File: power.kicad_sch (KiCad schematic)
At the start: 60 parts, among them J4 Conn_01x02, J5 Conn_01x02, J6 Conn_01x02, Q29 AO3401, Q30 Q_NPN_BEC, T1 COMMON_MODE_CHOKE, U14 NJM2845DL1-3.3, U19 TPS54428DDA, U2 TPS54202

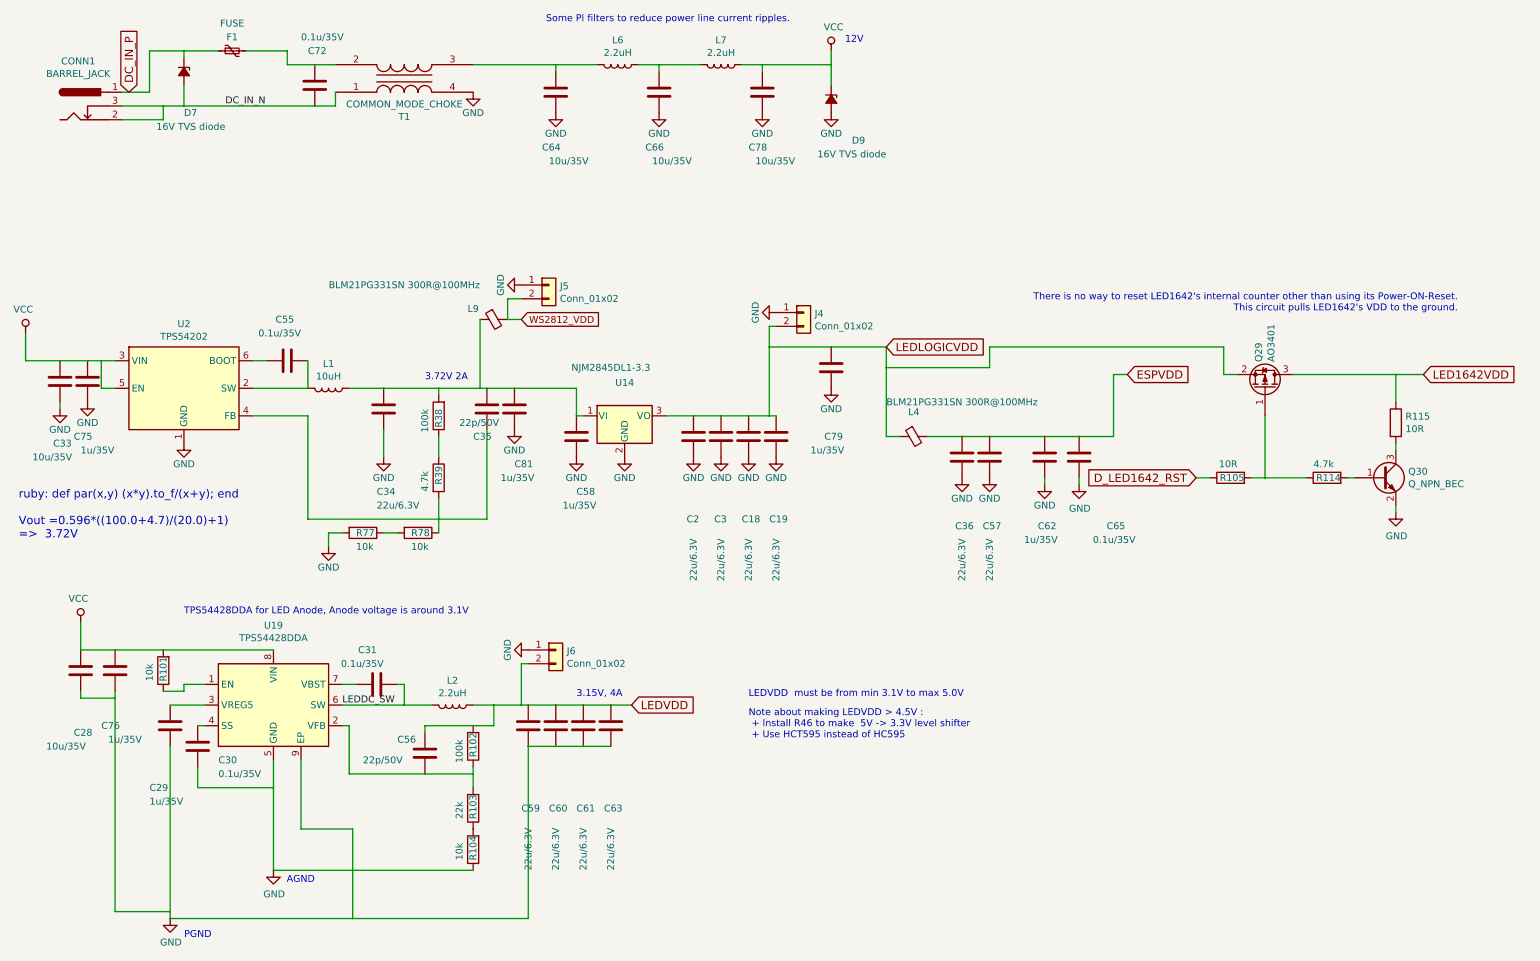
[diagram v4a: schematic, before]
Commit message: Added a schematic comments; I don't know why other files are updated
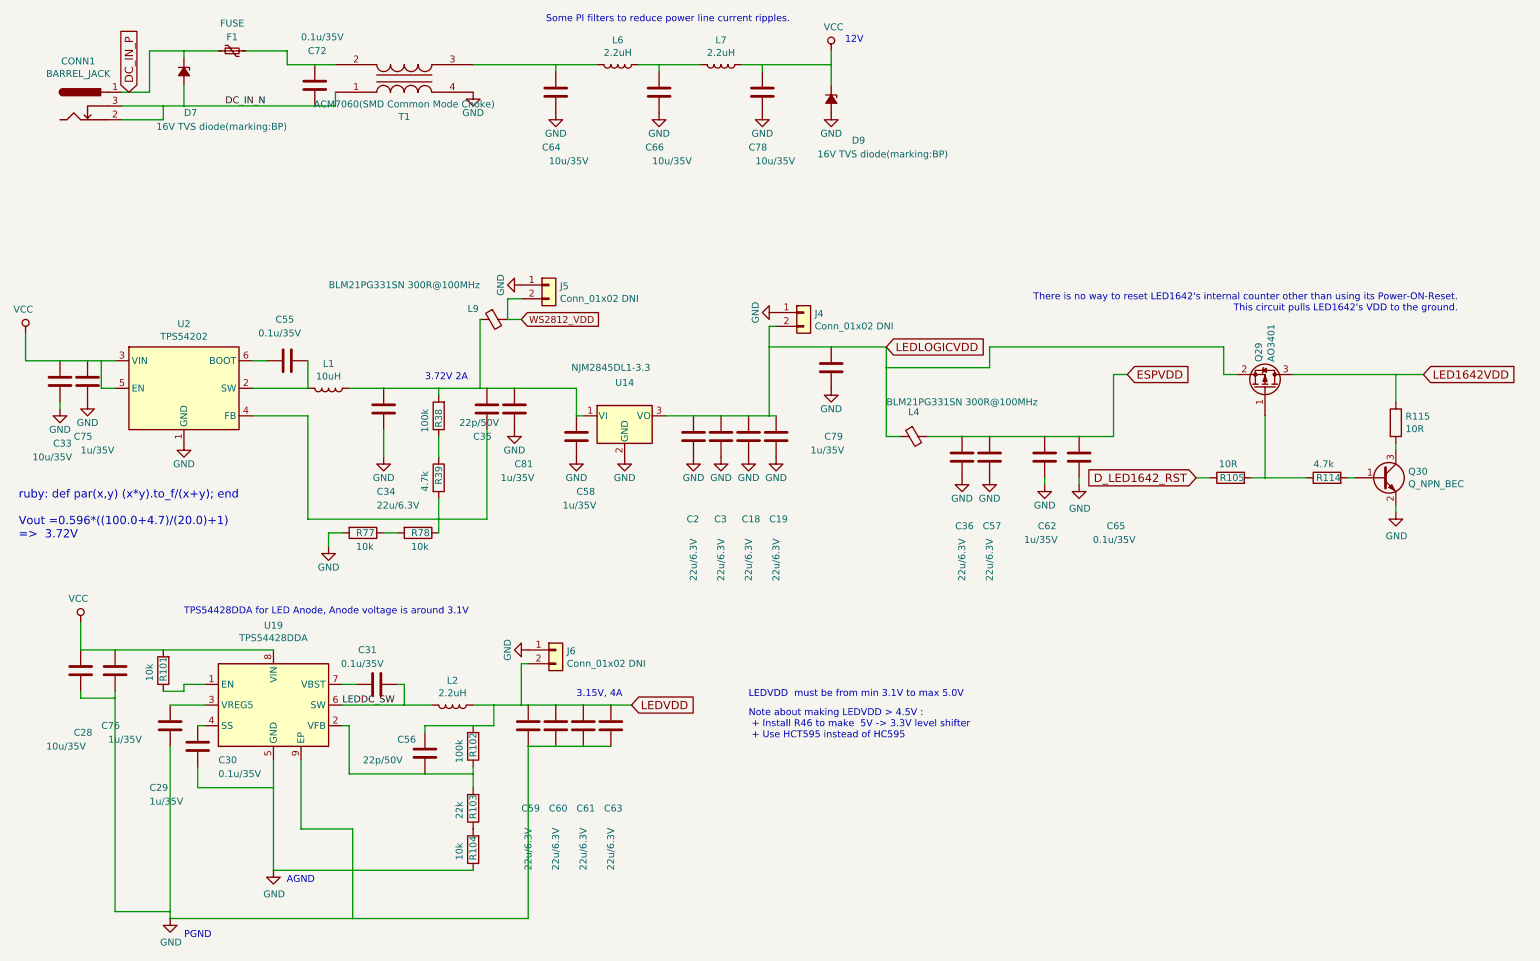
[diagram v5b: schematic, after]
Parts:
- D7, D9: value 16V TVS diode -> 16V TVS diode(marking:BP)
- J4, J5, J6: value Conn_01x02 -> Conn_01x02 DNI
- T1: value COMMON_MODE_CHOKE -> ACM7060(SMD Common Mode Choke)
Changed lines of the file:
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@@
 (kicad_sch (version 20201015) (generator eeschema)
-  (page 1 10)
   (paper "A4")
   (junction (at 21.59 81.28) (diameter 0.3048) (color 0 0 0 0))
@@
     (effects (font (size 1.27 1.27)) (justify left bottom))
   )
-  (global_label "DC_IN_P" (shape input) (at 34.29 31.75 90)
+  (global_label "DC_IN_P" (shape input) (at 34.29 31.75 90)    (property "Intersheet References" "${INTERSHEET_REFS}" (id 0) (at 0 0 0)
+      (effects (font (size 1.27 1.27)) hide)
+    )
     (effects (font (size 1.524 1.524)) (justify left))
   )
-  (global_label "WS2812_VDD" (shape input) (at 106.68 73.66 0)
+  (global_label "WS2812_VDD" (shape input) (at 106.68 73.66 0)    (property "Intersheet References" "${INTERSHEET_REFS}" (id 0) (at 0 0 0)
+      (effects (font (size 1.27 1.27)) hide)
+    )
     (effects (font (size 1.27 1.27)) (justify left))
   )
-  (global_label "LEDVDD" (shape input) (at 127 144.78 0)
+  (global_label "LEDVDD" (shape input) (at 127 144.78 0)    (property "Intersheet References" "${INTERSHEET_REFS}" (id 0) (at 0 0 0)
+      (effects (font (size 1.27 1.27)) hide)
+    )
     (effects (font (size 1.524 1.524)) (justify left))
   )
-  (global_label "LEDLOGICVDD" (shape input) (at 173.99 78.74 0)
+  (global_label "LEDLOGICVDD" (shape input) (at 173.99 78.74 0)    (property "Intersheet References" "${INTERSHEET_REFS}" (id 0) (at 0 0 0)
+      (effects (font (size 1.27 1.27)) hide)
+    )
     (effects (font (size 1.524 1.524)) (justify left))
   )
-  (global_label "ESPVDD" (shape input) (at 218.44 83.82 0)
+  (global_label "ESPVDD" (shape input) (at 218.44 83.82 0)    (property "Intersheet References" "${INTERSHEET_REFS}" (id 0) (at 0 0 0)
+      (effects (font (size 1.27 1.27)) hide)
+    )
     (effects (font (size 1.524 1.524)) (justify left))
   )
-  (global_label "D_LED1642_RST" (shape input) (at 231.14 102.87 180)
+  (global_label "D_LED1642_RST" (shape input) (at 231.14 102.87 180)    (property "Intersheet References" "${INTERSHEET_REFS}" (id 0) (at 0 0 0)
+      (effects (font (size 1.27 1.27)) hide)
+    )
     (effects (font (size 1.524 1.524)) (justify right))
   )
-  (global_label "LED1642VDD" (shape input) (at 273.05 83.82 0)
+  (global_label "LED1642VDD" (shape input) (at 273.05 83.82 0)    (property "Intersheet References" "${INTERSHEET_REFS}" (id 0) (at 0 0 0)
+      (effects (font (size 1.27 1.27)) hide)
+    )
     (effects (font (size 1.524 1.524)) (justify left))
   )
@@
       (effects (font (size 1.27 1.27)) (justify left))
     )
-    (property "Value" "16V TVS diode" (id 1) (at 39.37 38.1 90)
+    (property "Value" "16V TVS diode(marking:BP)" (id 1) (at 39.37 38.1 90)
       (effects (font (size 1.27 1.27)) (justify left))
     )
@@
       (effects (font (size 1.27 1.27)) (justify left))
     )
-    (property "Value" "16V TVS diode" (id 1) (at 161.29 43.18 90)
+    (property "Value" "16V TVS diode(marking:BP)" (id 1) (at 161.29 43.18 90)
       (effects (font (size 1.27 1.27)) (justify left))
     )
@@
       (effects (font (size 1.27 1.27)) (justify left))
     )
-    (property "Value" "Conn_01x02" (id 1) (at 113.792 69.8246 0)
+    (property "Value" "Conn_01x02 DNI" (id 1) (at 113.792 69.825 0)
       (effects (font (size 1.27 1.27)) (justify left))
     )
@@
       (effects (font (size 1.27 1.27)) (justify left))
     )
-    (property "Value" "Conn_01x02" (id 1) (at 115.062 137.1346 0)
+    (property "Value" "Conn_01x02 DNI" (id 1) (at 115.062 137.135 0)
       (effects (font (size 1.27 1.27)) (justify left))
     )
@@
       (effects (font (size 1.27 1.27)) (justify left))
     )
-    (property "Value" "Conn_01x02" (id 1) (at 160.782 74.9046 0)
+    (property "Value" "Conn_01x02 DNI" (id 1) (at 160.782 74.905 0)
       (effects (font (size 1.27 1.27)) (justify left))
     )
@@
     (in_bom yes) (on_board yes)
     (property "Reference" "T1" (id 0) (at 85.09 36.2712 0))
-    (property "Value" "COMMON_MODE_CHOKE" (id 1) (at 85.09 33.9598 0))
+    (property "Value" "ACM7060(SMD Common Mode Choke)" (id 1) (at 85.09 33.9598 0))
     (property "Footprint" "components:Choke_COMMON_SMD_ACM7060" (id 2) (at 85.09 29.21 90)
       (effects (font (size 1.27 1.27)) hide)

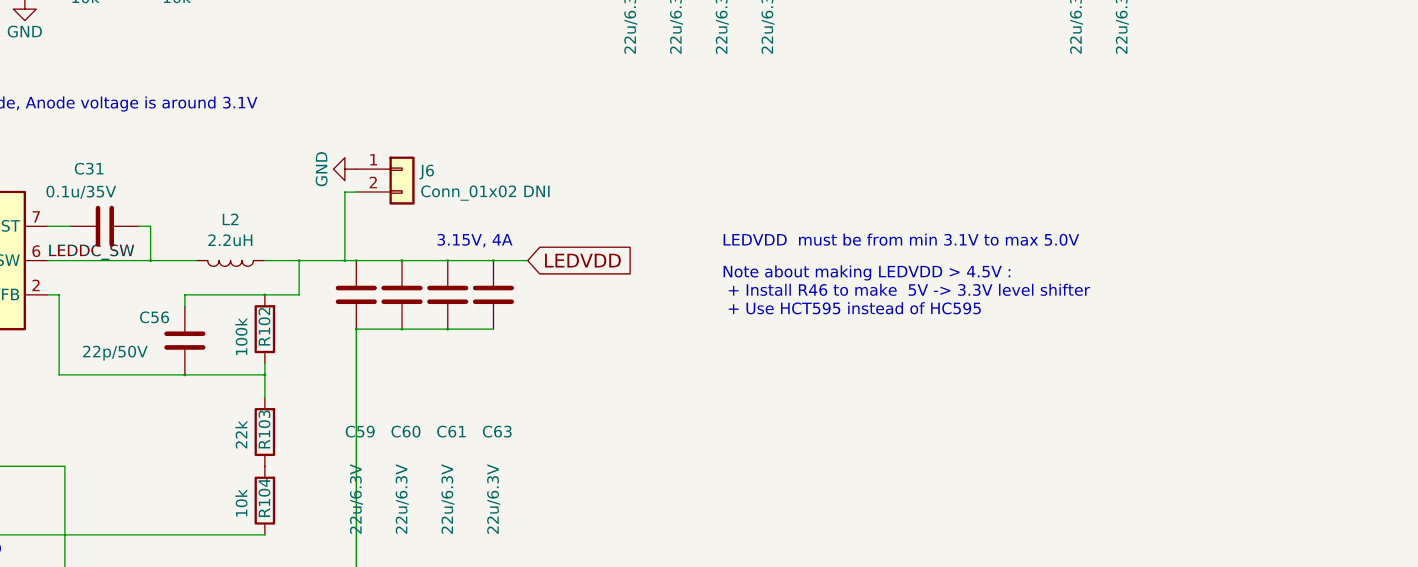
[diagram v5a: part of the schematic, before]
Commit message: Changed L2 value from 2.2uH to '2.2 ~ 6.8uH'
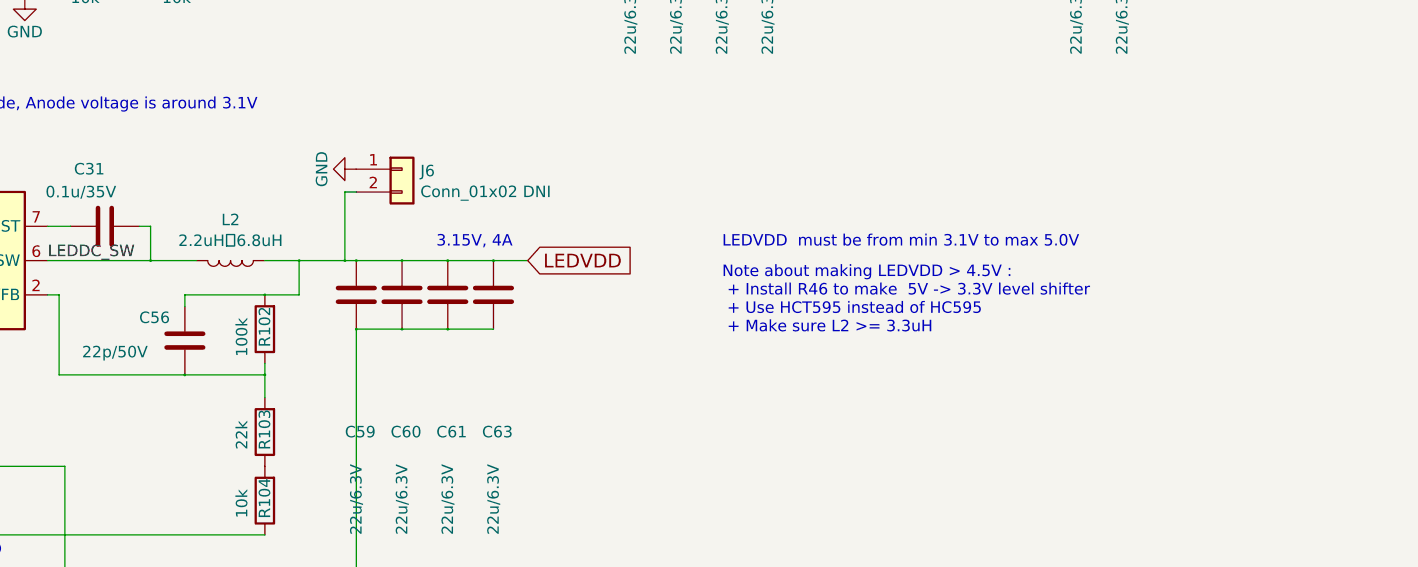
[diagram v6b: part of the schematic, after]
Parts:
- L2: value 2.2uH -> 2.2uH〜6.8uH
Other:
- note added: "Note about making LEDVDD > 4.5V : + Install R46 to make 5V -> 3.3V level shifter + Use HCT595 instead of HC595 + Make sure L2 >= 3.3uH"
- note removed: "Note about making LEDVDD > 4.5V : + Install R46 to make 5V -> 3.3V level shifter + Use HCT595 instead of HC595"

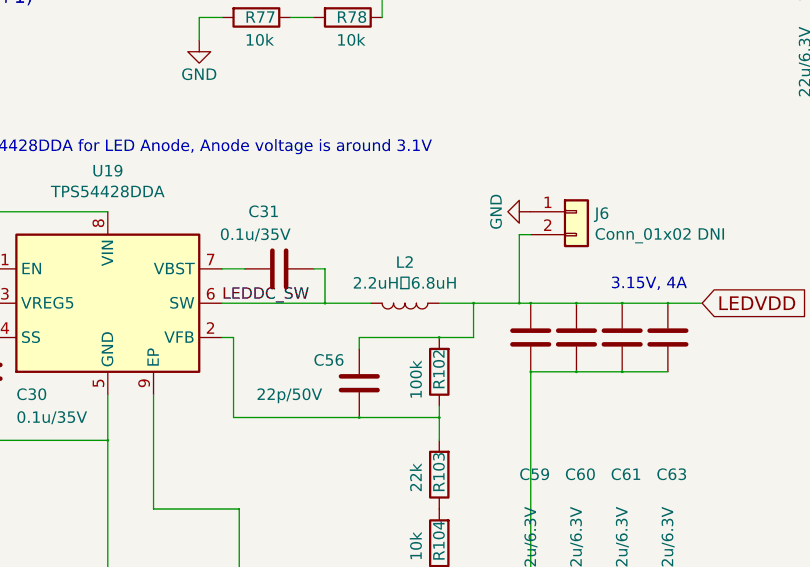
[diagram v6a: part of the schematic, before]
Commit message: Settled L2 value to 6.8uH
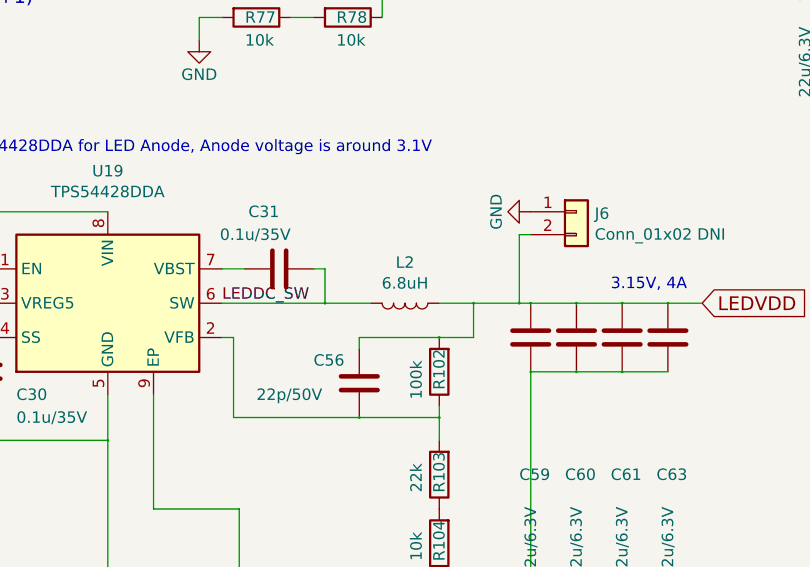
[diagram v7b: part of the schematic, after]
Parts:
- L2: value 2.2uH〜6.8uH -> 6.8uH
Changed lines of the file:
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@@
     (in_bom yes) (on_board yes)
     (property "Reference" "L2" (id 0) (at 93.98 140.2588 90))
-    (property "Value" "2.2uH〜6.8uH" (id 1) (at 93.98 142.57 90))
+    (property "Value" "6.8uH" (id 1) (at 93.98 142.57 90))
     (property "Footprint" "components:Choke_SMD_10.4x10.4_H4.8_HandSoldering" (id 2) (at 93.98 144.78 0)
       (effects (font (size 1.27 1.27)) hide)

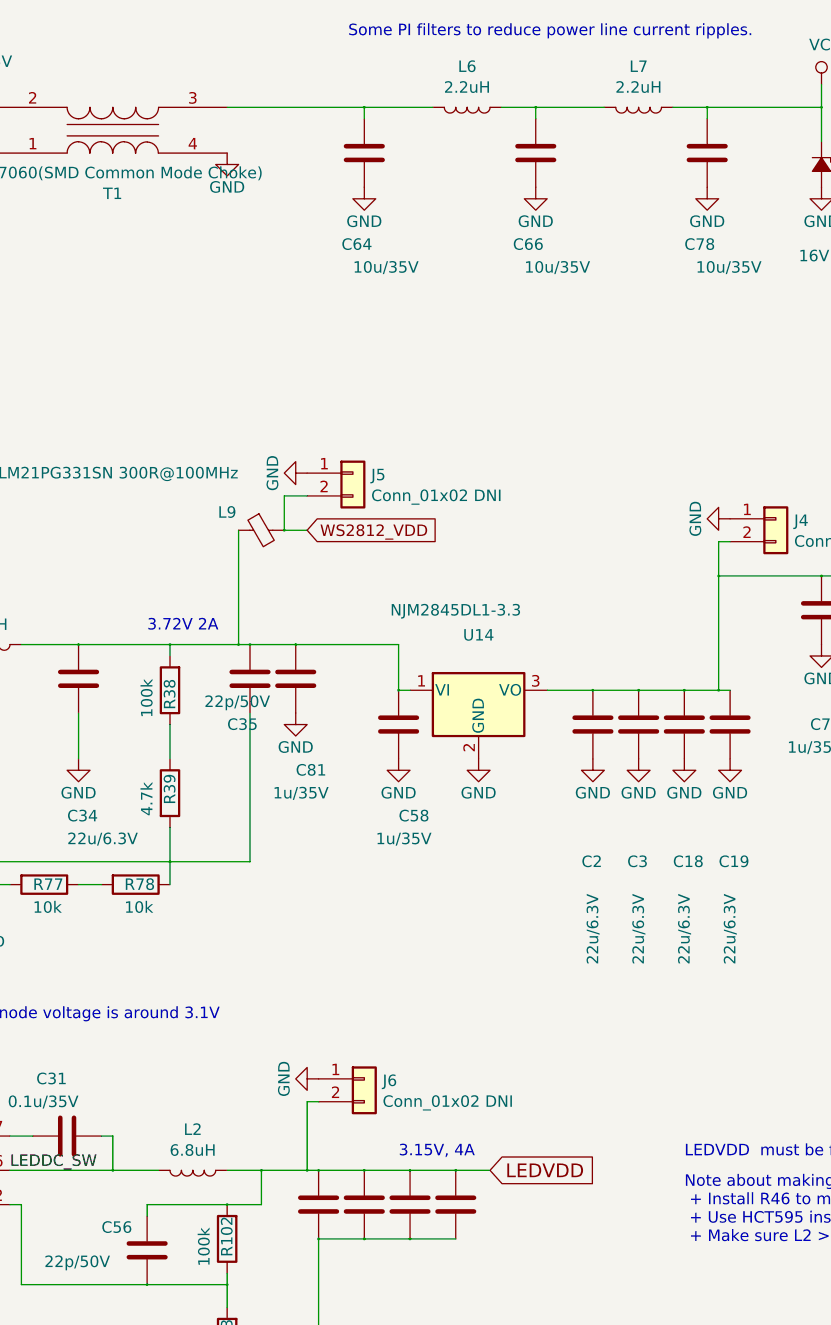
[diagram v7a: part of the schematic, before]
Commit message: Reverted L2 value from '6.8u' to '2.2u'. Instead, L7 has changed its value from '2.2u' to '6.8u' to preserve total component BOM. The reason is sound noise from L2.
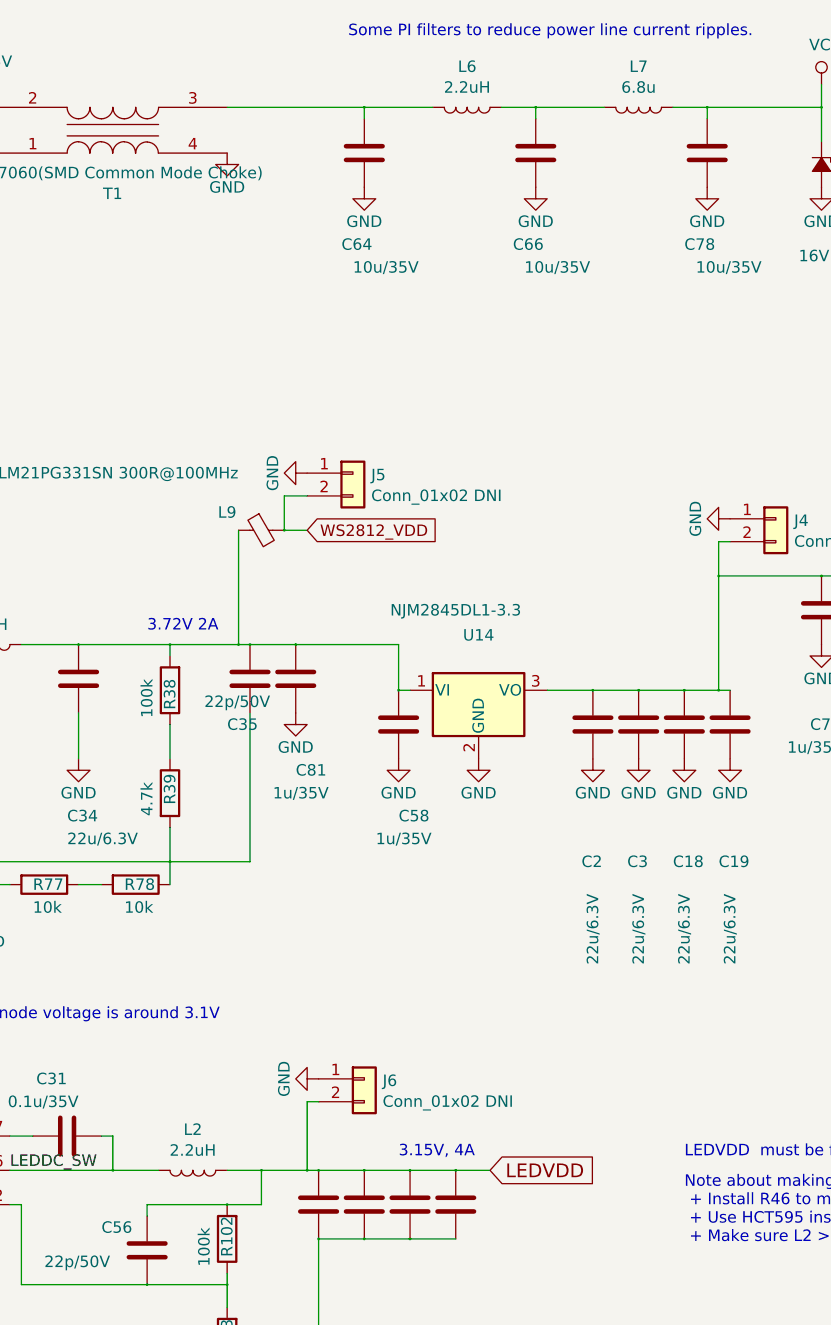
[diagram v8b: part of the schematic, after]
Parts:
- L2: value 6.8uH -> 2.2uH
- L7: value 2.2uH -> 6.8u
